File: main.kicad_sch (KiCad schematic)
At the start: 0 parts

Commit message: Working on schematic and layout
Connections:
- no-connect marks 1 -> 2
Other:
- added sheet io (io.kicad_sch)
- sheet boost_a_control ports: added VOUT_IN; removed none
- sheet boost_a_in_sns ports: added I2C_SETTING; removed none
- sheet boost_b_control ports: added VOUT_IN; removed none
- sheet boost_b_in_sns ports: added I2C_SETTING; removed none
- sheet mcu ports: added BATT1{SIG_LSW}, BATT2{SIG_LSW}, BOOT, NAV1{SIG_NAV_LSW}, NAV2{SIG_NAV_LSW}, RUN, USB_D+, USB_D-, {SERIAL}; removed SX{SIG_LSW}, SY{SIG_LSW}
- sheet navlight_load_sw1 ports: added {SIG_NAV_LSW}; removed GPIO_IN, nFLT
- sheet navlight_load_sw2 ports: added {SIG_NAV_LSW}; removed GPIO_IN, nFLT

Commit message: Working on layout
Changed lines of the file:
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@@
 		)
 	)
-	(label "NAV1{SIG_NAV_LSW}"
+	(label "NAV2{SIG_NAV_LSW}"
 		(at 243.84 151.13 0)
 		(effects
@@
 		)
 	)
-	(label "NAV1{SIG_NAV_LSW}"
+	(label "NAV2{SIG_NAV_LSW}"
 		(at 290.83 151.13 180)
 		(effects
@@
 			)
 		)
-		(pin "NAV1{SIG_NAV_LSW}" bidirectional
-			(at 242.57 151.13 0)
-			(effects
-				(font
-					(size 1.27 1.27)
-				)
-				(justify right)
-			)
-		)
-		(pin "NAV2{SIG_NAV_LSW}" bidirectional
-			(at 242.57 146.05 0)
-			(effects
-				(font
-					(size 1.27 1.27)
-				)
-				(justify right)
-			)
-		)
 		(pin "{SERIAL}" bidirectional
 			(at 196.85 154.94 180)
@@
 			)
 		)
+		(pin "NAV1{SIG_NAV_LSW}" bidirectional
+			(at 242.57 146.05 0)
+			(effects
+				(font
+					(size 1.27 1.27)
+				)
+				(justify right)
+			)
+		)
+		(pin "NAV2{SIG_NAV_LSW}" bidirectional
+			(at 242.57 151.13 0)
+			(effects
+				(font
+					(size 1.27 1.27)
+				)
+				(justify right)
+			)
+		)

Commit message: Pushing
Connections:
- no-connect marks 2 -> 0
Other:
- sheet boost_a_control ports: added I2C_SETTING; removed none
- sheet boost_b_control ports: added I2C_SETTING; removed none
- sheet mcu ports: added A_SENSE_ALERT, B_SENSE_ALERT; removed none

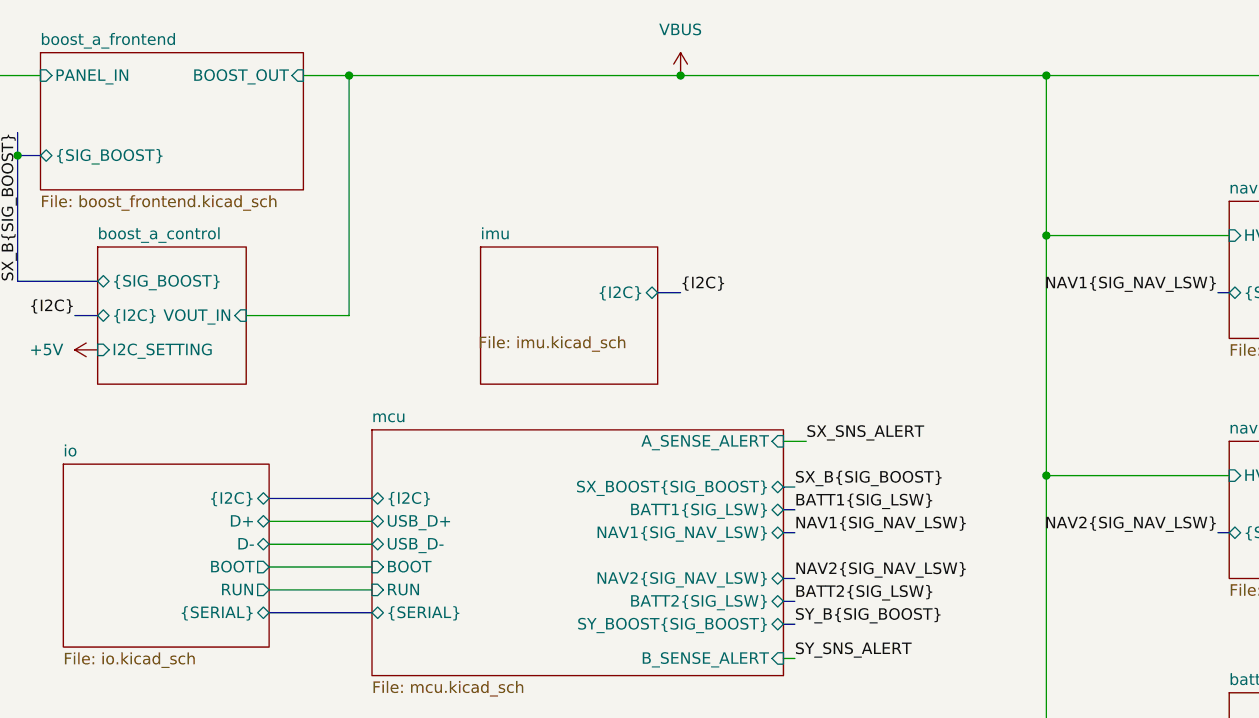
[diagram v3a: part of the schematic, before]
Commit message: Schematic updates
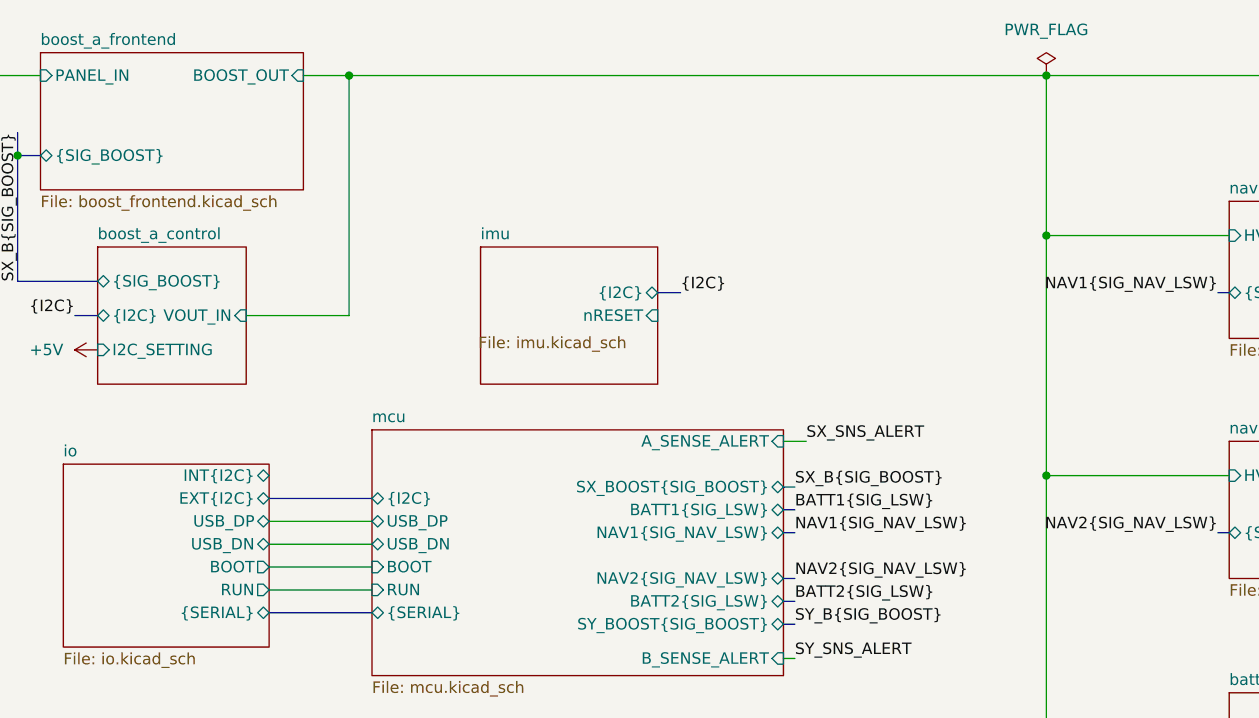
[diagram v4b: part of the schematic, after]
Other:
- sheet imu ports: added nRESET; removed none
- sheet io ports: added EXT{I2C}, INT{I2C}, USB_DN, USB_DP; removed D+, D-, {I2C}
- sheet mcu ports: added USB_DN, USB_DP; removed USB_D+, USB_D-
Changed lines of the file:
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@@
-	)
-	(junction
-		(at 231.14 100.33)
-		(diameter 0)
-		(color 0 0 0 0)
 	)
 	(junction
@@
 	(wire
 		(pts
-			(xy 231.14 100.33) (xy 271.78 100.33)
+			(xy 194.31 100.33) (xy 271.78 100.33)
 		)
 		(stroke
@@
 		(pts
 			(xy 157.48 109.22) (xy 157.48 123.19)
-		)
-		(stroke
-			(width 0)
-			(type default)
-		)
-	)
-	(wire
-		(pts
-			(xy 194.31 100.33) (xy 231.14 100.33)
 		)
 		(stroke
@@
 	)
 	(symbol
+		(lib_id "power:PWR_FLAG")
+		(at 271.78 100.33 0)
+		(unit 1)
+		(exclude_from_sim no)
+		(in_bom yes)
+		(on_board yes)
+		(dnp no)
+		(fields_autoplaced yes)
+		(property "Reference" "#FLG02"
+			(at 271.78 98.425 0)
+			(effects
+				(font
+					(size 1.27 1.27)
+				)
+				(hide yes)
+			)
+		)
+		(property "Value" "PWR_FLAG"
+			(at 271.78 95.25 0)
+			(effects
+				(font
+					(size 1.27 1.27)
+				)
+			)
+		)
+		(property "Footprint" ""
+			(at 271.78 100.33 0)
+			(effects
+				(font
+					(size 1.27 1.27)
+				)
+				(hide yes)
+			)
+		)
+		(property "Datasheet" "~"
+			(at 271.78 100.33 0)
+			(effects
+				(font
+					(size 1.27 1.27)
+				)
+				(hide yes)
+			)
+		)
+		(property "Description" "Special symbol for telling ERC where power comes from"
+			(at 271.78 100.33 0)
+			(effects
+				(font
+					(size 1.27 1.27)
+				)
+				(hide yes)
+			)
+		)
+		(pin "1"
+		)
+		(instances
+			(project ""
+				(path "/99785679-20de-4827-b4cc-bc3c187068c9/9564929a-642e-4163-88c2-45054b63a5ed"
+					(reference "#FLG02")
+					(unit 1)
+				)
+			)
+		)
+	)
+	(symbol
 		(lib_id "power:+5V")
 		(at 115.57 104.14 270)
@@
 				(path "/99785679-20de-4827-b4cc-bc3c187068c9/9564929a-642e-4163-88c2-45054b63a5ed"
 					(reference "#PWR0153")
-					(unit 1)
-				)
-			)
-		)
-	)
-	(symbol
-		(lib_id "power:VBUS")
-		(at 231.14 100.33 0)
-		(unit 1)
-		(exclude_from_sim no)
-		(in_bom yes)
-		(on_board yes)
-		(dnp no)
-		(fields_autoplaced yes)
-		(property "Reference" "#PWR03"
-			(at 231.14 104.14 0)
-			(effects
-				(font
-					(size 1.27 1.27)
-				)
-				(hide yes)
-			)
-		)
-		(property "Value" "VBUS"
-			(at 231.14 95.25 0)
-			(effects
-				(font
-					(size 1.27 1.27)
-				)
-			)
-		)
-		(property "Footprint" ""
-			(at 231.14 100.33 0)
-			(effects
-				(font
-					(size 1.27 1.27)
-				)
-				(hide yes)
-			)
-		)
-		(property "Datasheet" ""
-			(at 231.14 100.33 0)
-			(effects
-				(font
-					(size 1.27 1.27)
-				)
-				(hide yes)
-			)
-		)
-		(property "Description" "Power symbol creates a global label with name \"VBUS\""
-			(at 231.14 100.33 0)
-			(effects
-				(font
-					(size 1.27 1.27)
-				)
-				(hide yes)
-			)
-		)
-		(pin "1"
-		)
-		(instances
-			(project ""
-				(path "/99785679-20de-4827-b4cc-bc3c187068c9/9564929a-642e-4163-88c2-45054b63a5ed"
-					(reference "#PWR03")
 					(unit 1)
 				)
@@
 			)
 		)
-		(pin "{I2C}" bidirectional
-			(at 185.42 147.32 0)
-			(effects
-				(font
-					(size 1.27 1.27)
-				)
-				(justify right)
-			)
-		)
-		(pin "D+" bidirectional
-			(at 185.42 149.86 0)
-			(effects
-				(font
-					(size 1.27 1.27)
-				)
-				(justify right)
-			)
-		)
-		(pin "D-" bidirectional
-			(at 185.42 152.4 0)
-			(effects
-				(font
-					(size 1.27 1.27)
-				)
-				(justify right)
-			)
-		)
 		(pin "{SERIAL}" bidirectional
 			(at 185.42 160.02 0)
@@
 		(pin "RUN" output
 			(at 185.42 157.48 0)
+			(effects
+				(font
+					(size 1.27 1.27)
+				)
+				(justify right)
+			)
+		)
+		(pin "EXT{I2C}" bidirectional
+			(at 185.42 147.32 0)
+			(effects
+				(font
+					(size 1.27 1.27)
+				)
+				(justify right)
+			)
+		)
+		(pin "INT{I2C}" bidirectional
+			(at 185.42 144.78 0)
+			(effects
+				(font
+					(size 1.27 1.27)
+				)
+				(justify right)
+			)
+		)
+		(pin "USB_DN" bidirectional
+			(at 185.42 152.4 0)
+			(effects
+				(font
+					(size 1.27 1.27)
+				)
+				(justify right)
+			)
+		)
+		(pin "USB_DP" bidirectional
+			(at 185.42 149.86 0)
 			(effects
 				(font
@@
 			)
 		)
+		(pin "nRESET" input
+			(at 228.6 127 0)
+			(effects
+				(font
+					(size 1.27 1.27)
+				)
+				(justify right)
+			)
+		)
 		(instances
 			(project "PowerBoard"
@@
 			)
 		)
-		(pin "USB_D+" bidirectional
-			(at 196.85 149.86 180)
-			(effects
-				(font
-					(size 1.27 1.27)
-				)
-				(justify left)
-			)
-		)
-		(pin "USB_D-" bidirectional
-			(at 196.85 152.4 180)
-			(effects
-				(font
-					(size 1.27 1.27)
-				)
-				(justify left)
-			)
-		)
 		(pin "{SERIAL}" bidirectional
 			(at 196.85 160.02 180)
@@
 			)
 		)
+		(pin "USB_DN" bidirectional
+			(at 196.85 152.4 180)
+			(effects
+				(font
+					(size 1.27 1.27)
+				)
+				(justify left)
+			)
+		)
+		(pin "USB_DP" bidirectional
+			(at 196.85 149.86 180)
+			(effects
+				(font
+					(size 1.27 1.27)
+				)
+				(justify left)
+			)
+		)

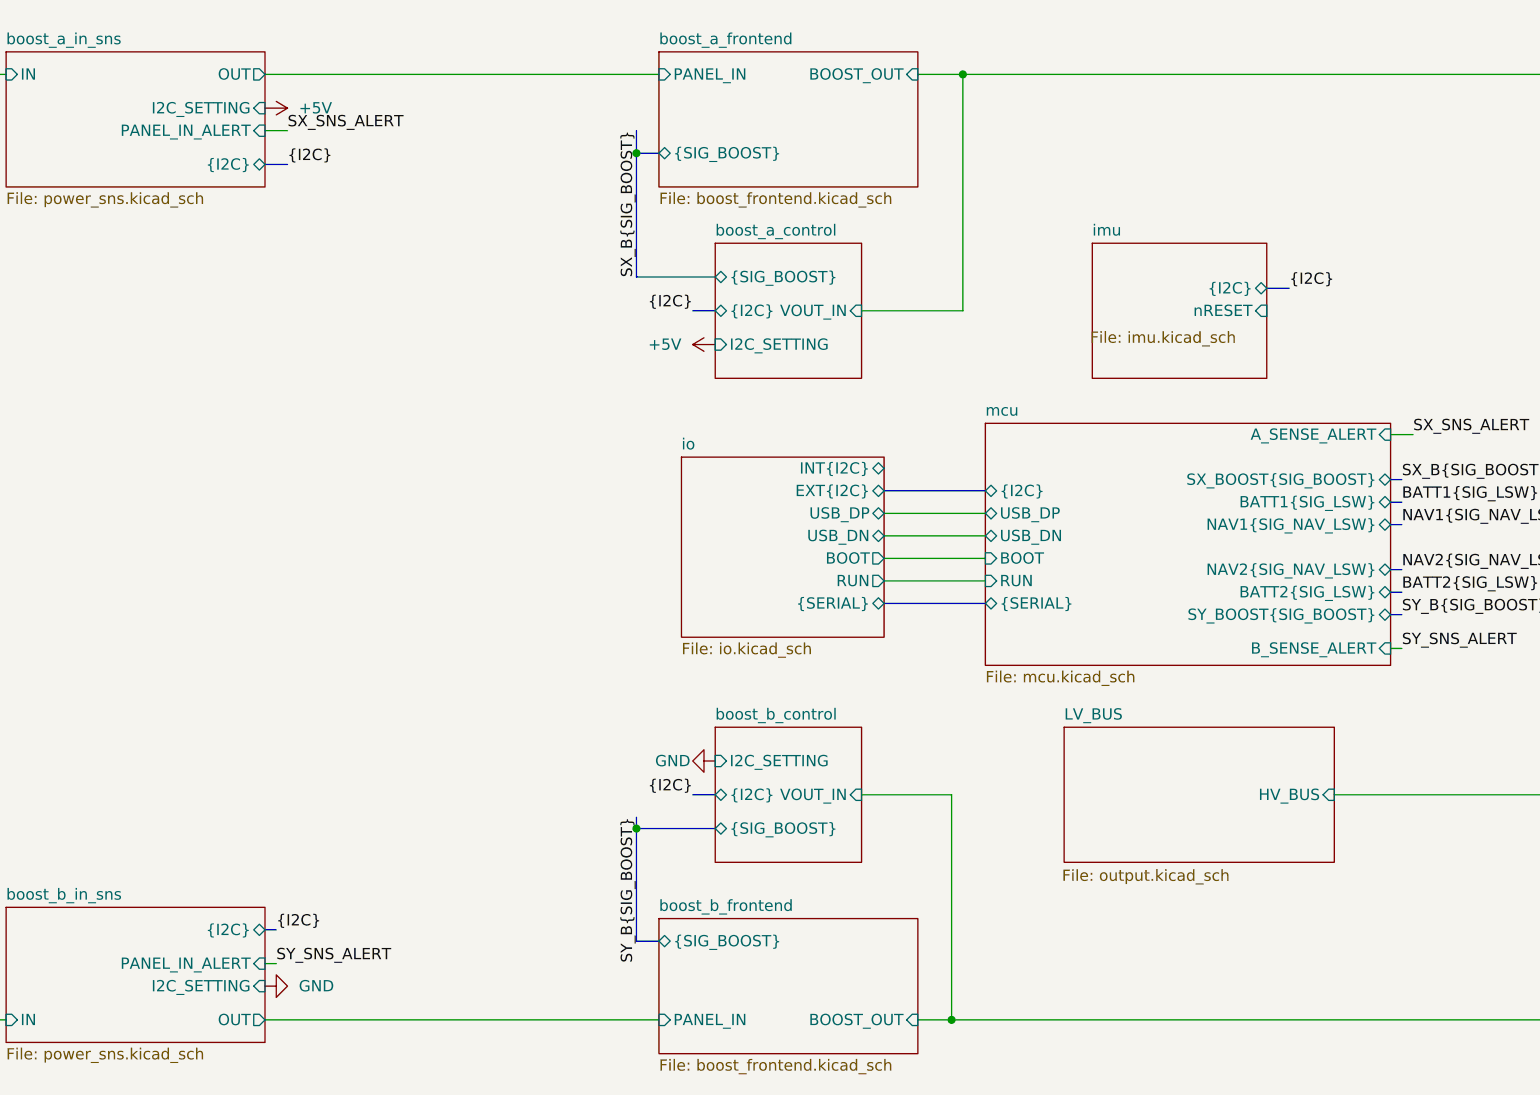
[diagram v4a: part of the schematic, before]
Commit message: i2c 0 and 1 bus routed + mosfet logic change
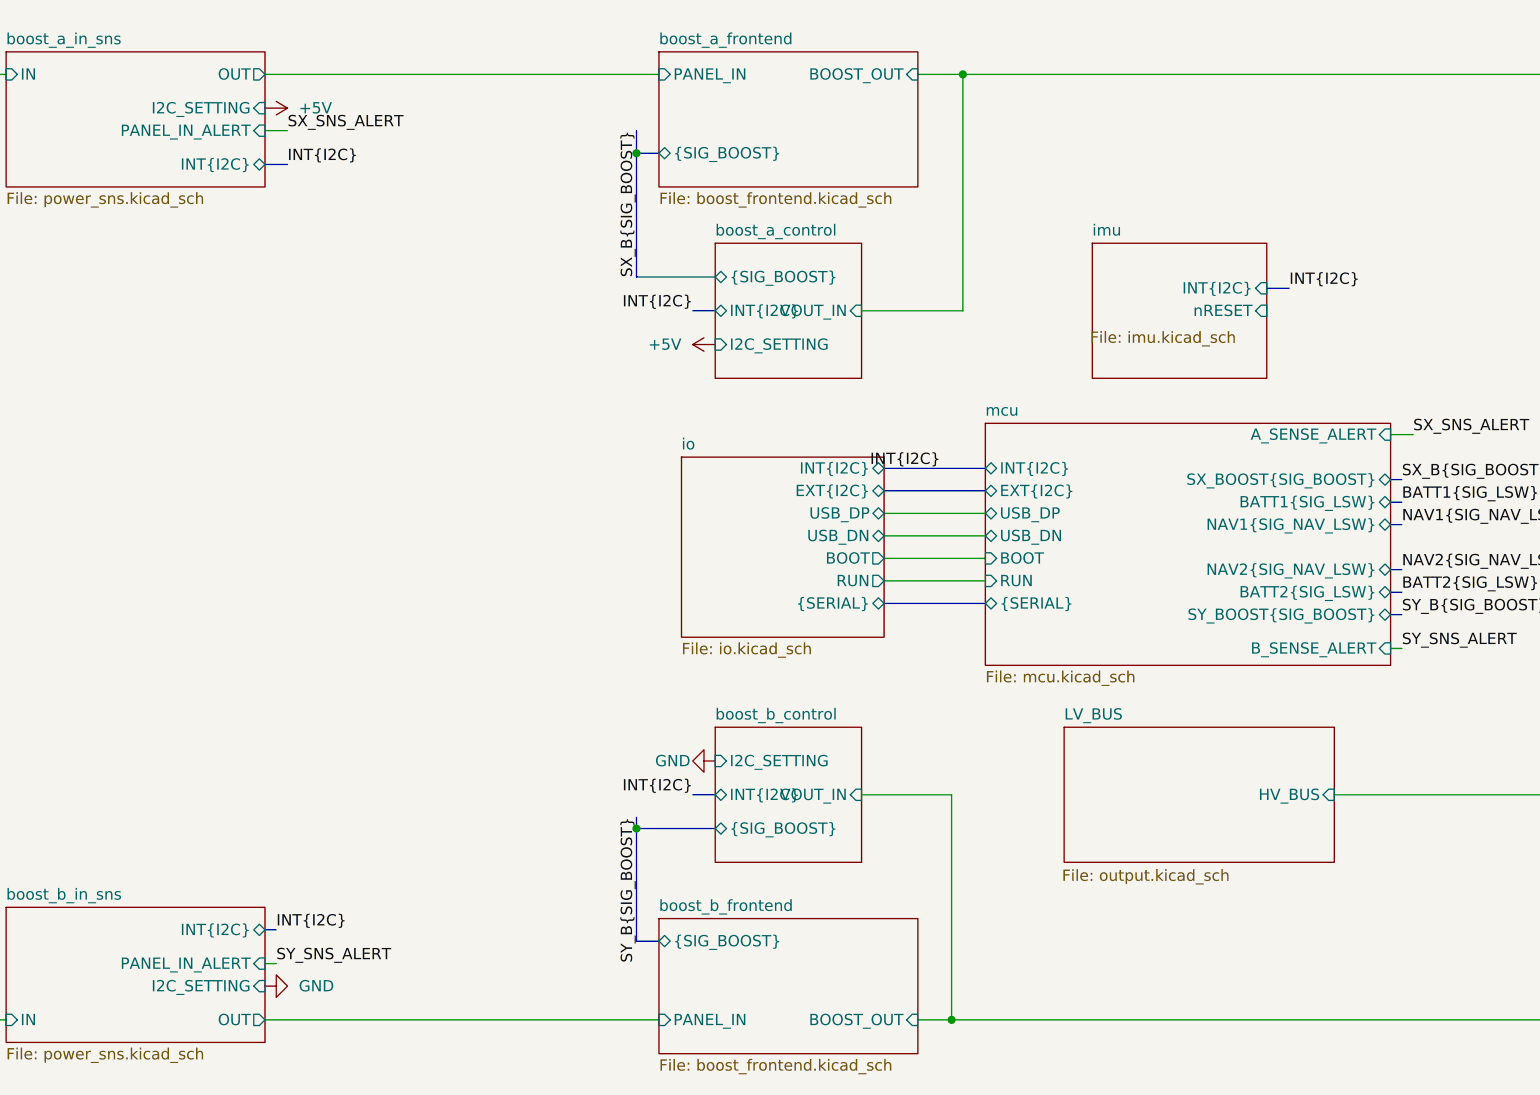
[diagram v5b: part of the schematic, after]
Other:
- sheet boost_a_control ports: added INT{I2C}; removed {I2C}
- sheet boost_a_in_sns ports: added INT{I2C}; removed {I2C}
- sheet boost_b_control ports: added INT{I2C}; removed {I2C}
- sheet boost_b_in_sns ports: added INT{I2C}; removed {I2C}
- sheet imu ports: added INT{I2C}; removed {I2C}
- sheet mcu ports: added EXT{I2C}, INT{I2C}; removed {I2C}
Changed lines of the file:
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@@
+		)
+	)
+	(bus
+		(pts
+			(xy 185.42 144.78) (xy 196.85 144.78)
+		)
+		(stroke
+			(width 0)
+			(type default)
 		)
 	)
@@
 		)
 	)
+	(label "INT{I2C}"
+		(at 116.84 196.85 0)
+		(effects
+			(font
+				(size 1.27 1.27)
+			)
+			(justify left bottom)
+		)
+	)
 	(label "NAV1{SIG_NAV_LSW}"
 		(at 290.83 124.46 180)
@@
 		)
 	)
-	(label "{I2C}"
+	(label "INT{I2C}"
 		(at 118.11 110.49 0)
 		(effects
@@
 		)
 	)
-	(label "{I2C}"
+	(label "INT{I2C}"
 		(at 163.83 127 180)
 		(effects
@@
 		)
 	)
-	(label "{I2C}"
+	(label "INT{I2C}"
 		(at 163.83 181.61 180)
 		(effects
@@
 		)
 	)
-	(label "{I2C}"
+	(label "INT{I2C}"
 		(at 231.14 124.46 0)
 		(effects
@@
 		)
 	)
-	(label "{I2C}"
-		(at 116.84 196.85 0)
-		(effects
-			(font
-				(size 1.27 1.27)
-			)
-			(justify left bottom)
+	(label "INT{I2C}"
+		(at 191.77 144.78 180)
+		(effects
+			(font
+				(size 1.27 1.27)
+			)
+			(justify right bottom)
 		)
 	)
@@
 			)
 		)
-		(pin "{I2C}" bidirectional
-			(at 166.37 127 180)
-			(effects
-				(font
-					(size 1.27 1.27)
-				)
-				(justify left)
-			)
-		)
 		(pin "{SIG_BOOST}" bidirectional
 			(at 166.37 123.19 180)
@@
 		(pin "I2C_SETTING" input
 			(at 166.37 130.81 180)
+			(effects
+				(font
+					(size 1.27 1.27)
+				)
+				(justify left)
+			)
+		)
+		(pin "INT{I2C}" bidirectional
+			(at 166.37 127 180)
 			(effects
 				(font
@@
 			)
 		)
-		(pin "{I2C}" bidirectional
+		(pin "INT{I2C}" bidirectional
 			(at 115.57 196.85 0)
 			(effects
@@
 			)
 		)
-		(pin "{I2C}" bidirectional
-			(at 228.6 124.46 0)
-			(effects
-				(font
-					(size 1.27 1.27)
-				)
-				(justify right)
-			)
-		)
 		(pin "nRESET" input
 			(at 228.6 127 0)
+			(effects
+				(font
+					(size 1.27 1.27)
+				)
+				(justify right)
+			)
+		)
+		(pin "INT{I2C}" input
+			(at 228.6 124.46 0)
 			(effects
 				(font
@@
 			)
 		)
-		(pin "{I2C}" bidirectional
-			(at 166.37 181.61 180)
-			(effects
-				(font
-					(size 1.27 1.27)
-				)
-				(justify left)
-			)
-		)
 		(pin "I2C_SETTING" input
 			(at 166.37 177.8 180)
+			(effects
+				(font
+					(size 1.27 1.27)
+				)
+				(justify left)
+			)
+		)
+		(pin "INT{I2C}" bidirectional
+			(at 166.37 181.61 180)
 			(effects
 				(font
@@
 			)
 		)
-		(pin "{I2C}" bidirectional
-			(at 196.85 147.32 180)
-			(effects
-				(font
-					(size 1.27 1.27)
-				)
-				(justify left)
-			)
-		)
 		(pin "SY_BOOST{SIG_BOOST}" bidirectional
 			(at 242.57 161.29 0)
@@
 		(pin "USB_DP" bidirectional
 			(at 196.85 149.86 180)
+			(effects
+				(font
+					(size 1.27 1.27)
+				)
+				(justify left)
+			)
+		)
+		(pin "EXT{I2C}" bidirectional
+			(at 196.85 147.32 180)
+			(effects
+				(font
+					(size 1.27 1.27)
+				)
+				(justify left)
+			)
+		)
+		(pin "INT{I2C}" bidirectional
+			(at 196.85 144.78 180)
 			(effects
 				(font
@@
 			)
 		)
-		(pin "{I2C}" bidirectional
+		(pin "INT{I2C}" bidirectional
 			(at 115.57 110.49 0)
 			(effects
